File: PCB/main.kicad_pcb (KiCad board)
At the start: 2 copper layers, 112.9 x 63.7 mm, 123 parts, among them K1 HK19F-DCxxV-SHC, Q1 BC807, Q10 BC817, Q11 BC817, Q12 TPCA8120,L1Q, Q13 BC817, Q14 BC817, Q15 BC817, Q16 TPCA8120,L1Q, Q17 BC817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

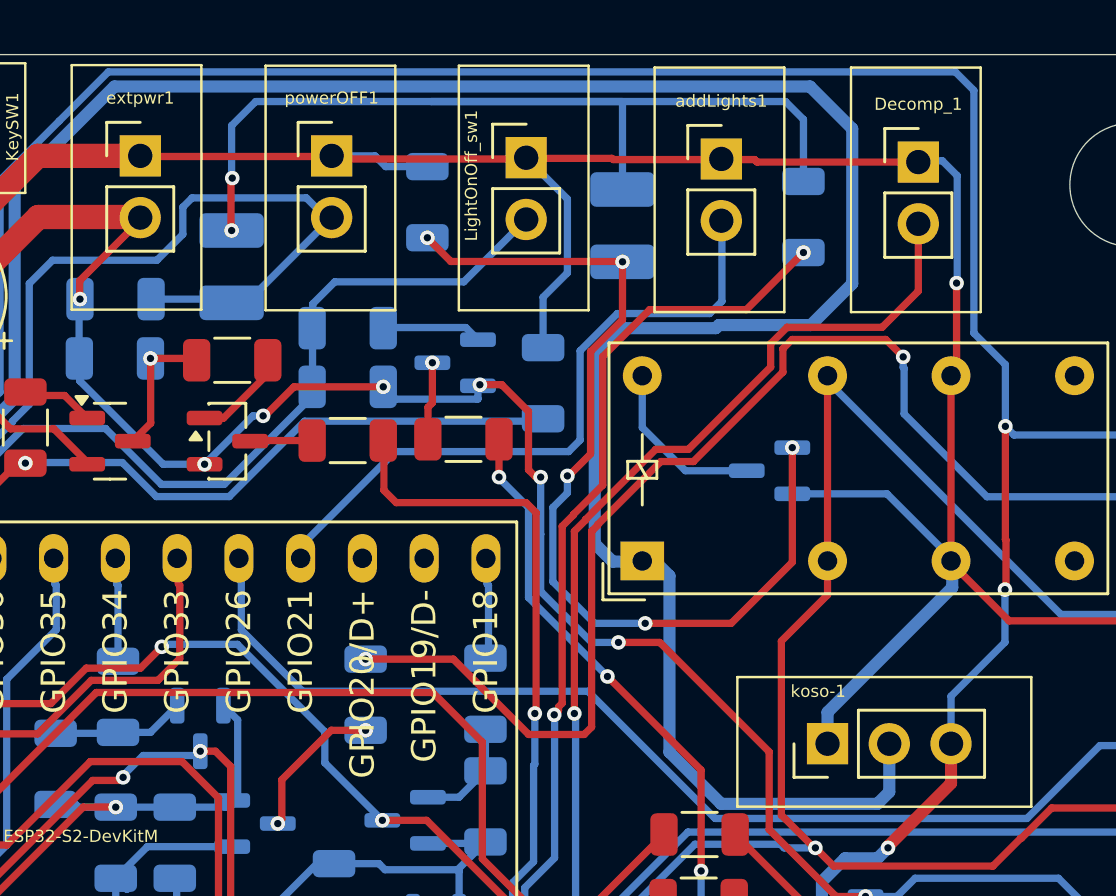
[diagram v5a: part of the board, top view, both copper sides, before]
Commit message: Fly back diode added to relay
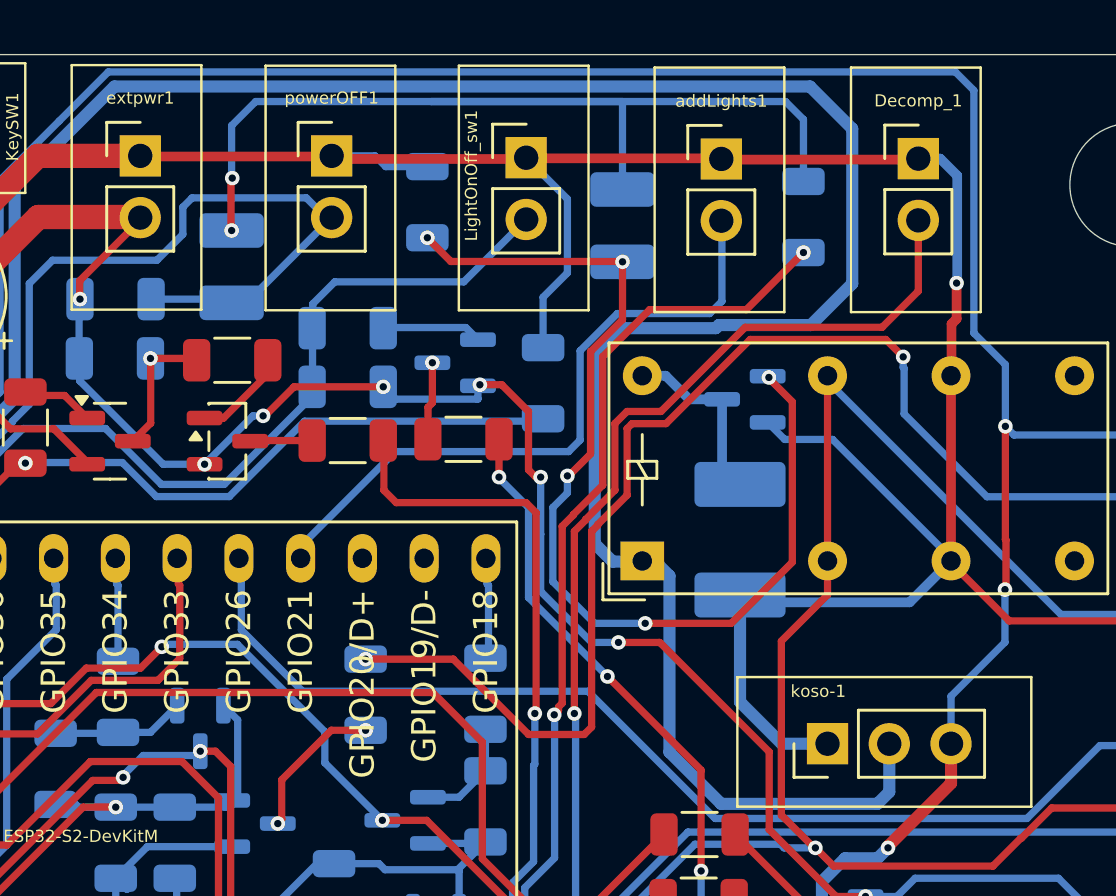
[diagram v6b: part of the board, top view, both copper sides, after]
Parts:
- added flyback-1: M7, Diode_SMD:D_2114_3652Metric_Pad1.85x3.75mm_HandSolder, B.Cu at (145.6, 73.7)
- moved Q4 3.11 mm to (145.8, 67.9)
- moved Decomp_1 0.14 mm to (152.9, 58.0)
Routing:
- net GND: track 470.5 -> 481.4 mm
- net Net-(D2-K): track 39.1 -> 42.5 mm
- net i_decompr: track 57.4 -> 58.6 mm
- net Net-(engReadyLed1-Pin_1): track 51.7 -> 52.7 mm

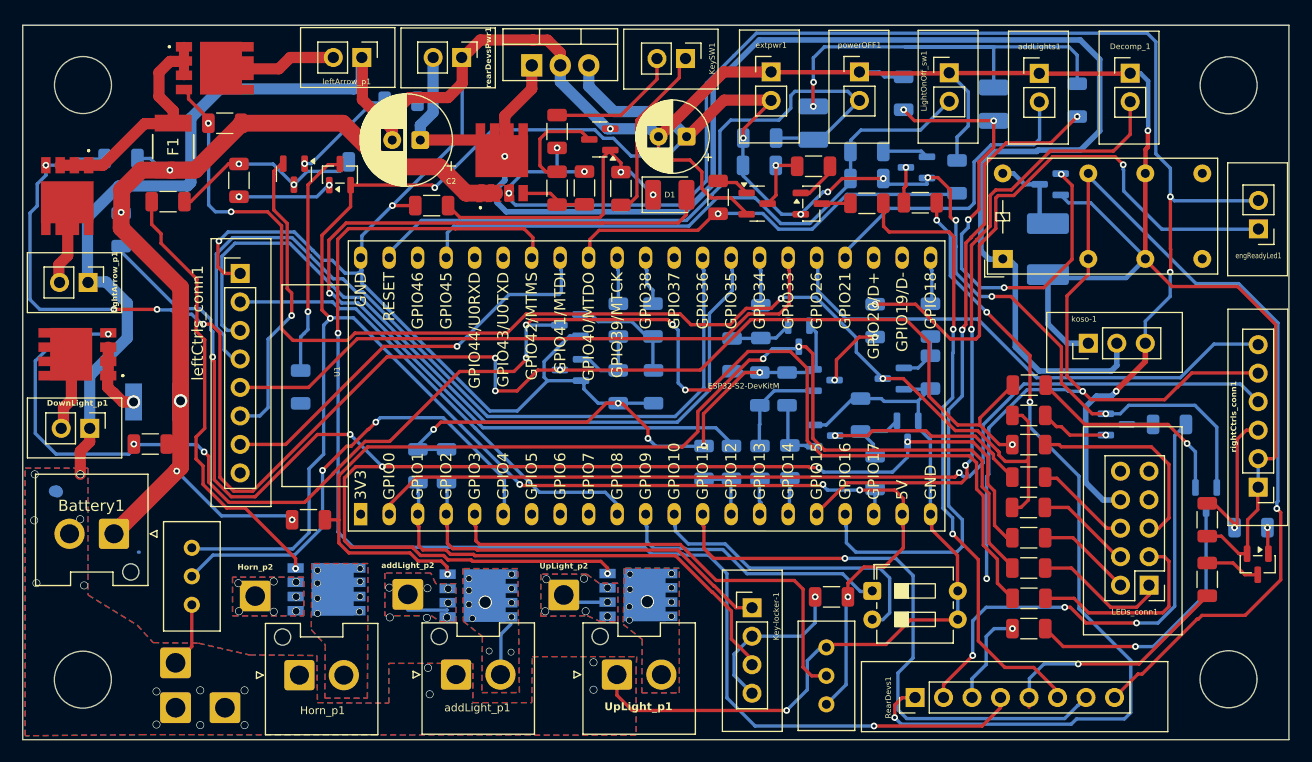
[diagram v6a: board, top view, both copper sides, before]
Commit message: Merge from ESP32__dualPCB
- Wrong diode footprints fixed
- Floating FET's source pin fixed
- Unuseful horn's propagation fixed
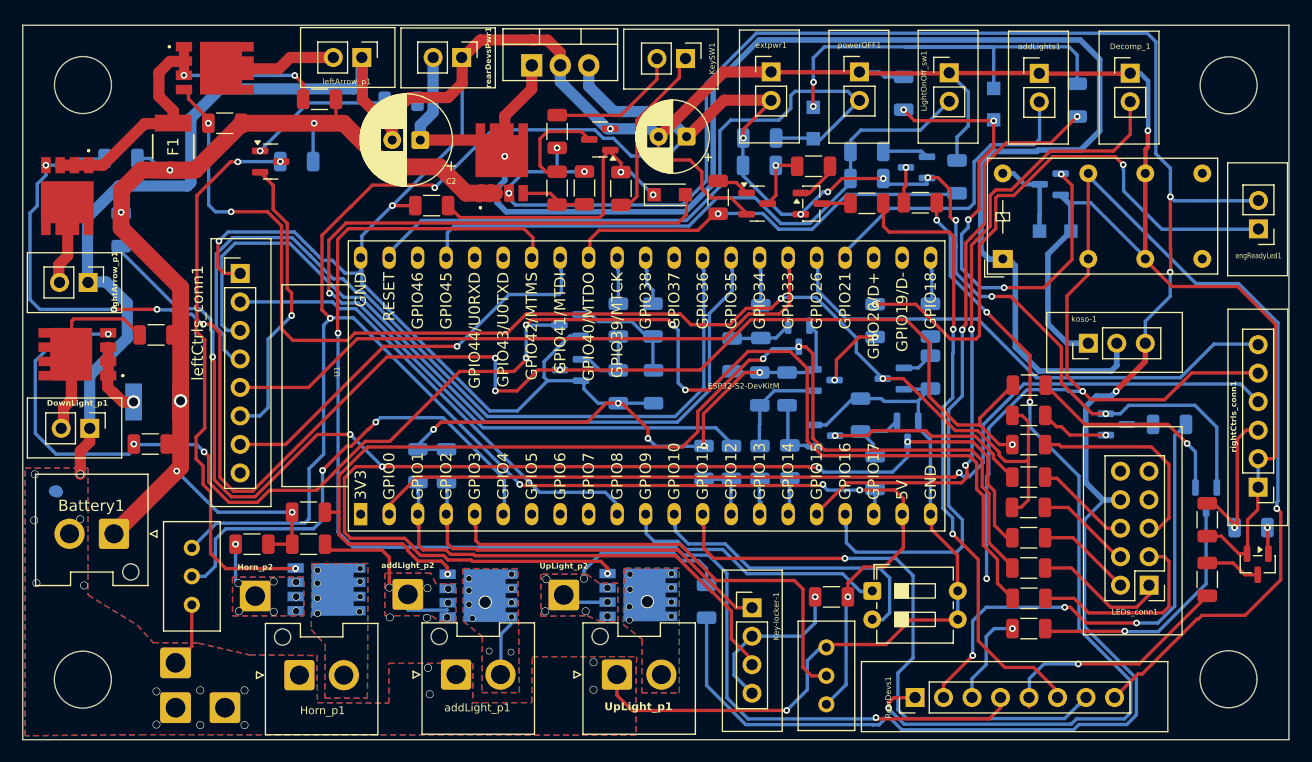
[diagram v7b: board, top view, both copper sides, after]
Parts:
- removed Q21: BC807, Package_TO_SOT_SMD:SOT-23
- removed RA26: 33K, Resistor_SMD:R_1206_3216Metric
- removed RA39: 10K, Resistor_SMD:R_1206_3216Metric
- removed RA45: 1K, Resistor_SMD:R_1206_3216Metric
- added RA15: 100K, Resistor_SMD:R_1206_3216Metric, F.Cu at (79.7, 100.0)
- added RA16: 100K, Resistor_SMD:R_1206_3216Metric, B.Cu at (115.2, 105.1)
- added RA17: 100K, Resistor_SMD:R_1206_3216Metric, F.Cu at (66.1, 81.3)
- added RA18: 100K, Resistor_SMD:R_1206_3216Metric, F.Cu at (80.7, 60.3)
- added RA19: 100K, Resistor_SMD:R_1206_3216Metric, F.Cu at (74.7, 100.0)
- D1, D2, D3: value D_Small -> PMEG40T30ER; footprint Diode_SMD:D_1210_3225Metric_Pad1.42x2.65mm_HandSolder -> Diode_SMD:Nexperia_CFP3_SOD-123W
- flyback-1: value M7 -> PMEG40T30ER; footprint Diode_SMD:D_2114_3652Metric_Pad1.85x3.75mm_HandSolder -> Diode_SMD:Nexperia_CFP3_SOD-123W
- moved RA21 6.10 mm to (78.7, 65.9)
- moved Q17 2.36 mm to (76.3, 65.9), turned to 0 degrees
- moved flyback-1 1.73 mm to (146.2, 72.1), turned to 0 degrees
- moved RA9 0.67 mm to (79.7, 97.1)
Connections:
- Q18 pad 4: Net-(Q18-G) -> Net-(Q17-C)
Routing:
- net +12V: track 226.5 -> 307.0 mm
- net Net-(Q18-G): track 39.7 -> 0.00 mm, vias 1 -> 0
- net Net-(Q17-C): track 17.6 -> 49.9 mm, vias 2 -> 3
- net Net-(Q21-C): track 20.4 -> 0.00 mm, vias 1 -> 0
- net Net-(Q6-S_1): track 3.76 -> 18.1 mm
- net Net-(Q12-S_1): track 21.9 -> 34.2 mm, vias 0 -> 2
- net Net-(DownLight_p1-Pin_2): track 6.98 -> 16.7 mm
- net Net-(Q5-S_1): track 3.58 -> 12.5 mm
- net Net-(Q21-B): track 8.48 -> 0.00 mm, vias 2 -> 0
- net Net-(Horn_p2-Pin_1): track 0.00 -> 3.58 mm, vias 7 -> 8
- net Net-(Q17-B): track 9.44 -> 12.9 mm
- net 5V: track 254.3 -> 252.4 mm
- net Net-(Q20-C): track 24.5 -> 22.9 mm
- net GND: track 481.4 -> 480.2 mm
- net Net-(U1-GPIO4/TOUCH4/ADC1_CH3): track 42.1 -> 43.1 mm
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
